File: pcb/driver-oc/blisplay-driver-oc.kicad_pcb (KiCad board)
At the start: 2 copper layers, 38 x 9 mm, 13 parts, among them J2 Flex, J3 Flex, J4 Flex, J5 Flex, U1 NCV7751

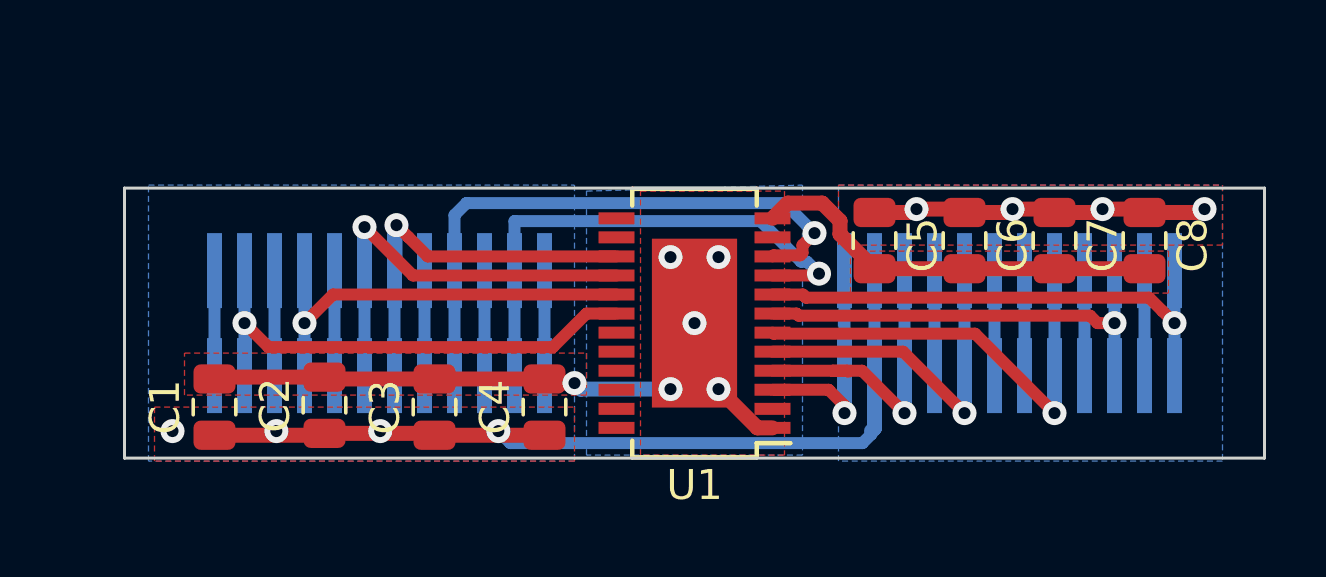
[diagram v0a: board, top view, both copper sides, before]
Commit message: Add simple connector to driver board.
This is not mirror symmetric which would be nicer for hassle-free
wiring. Maybe there should be two variants.
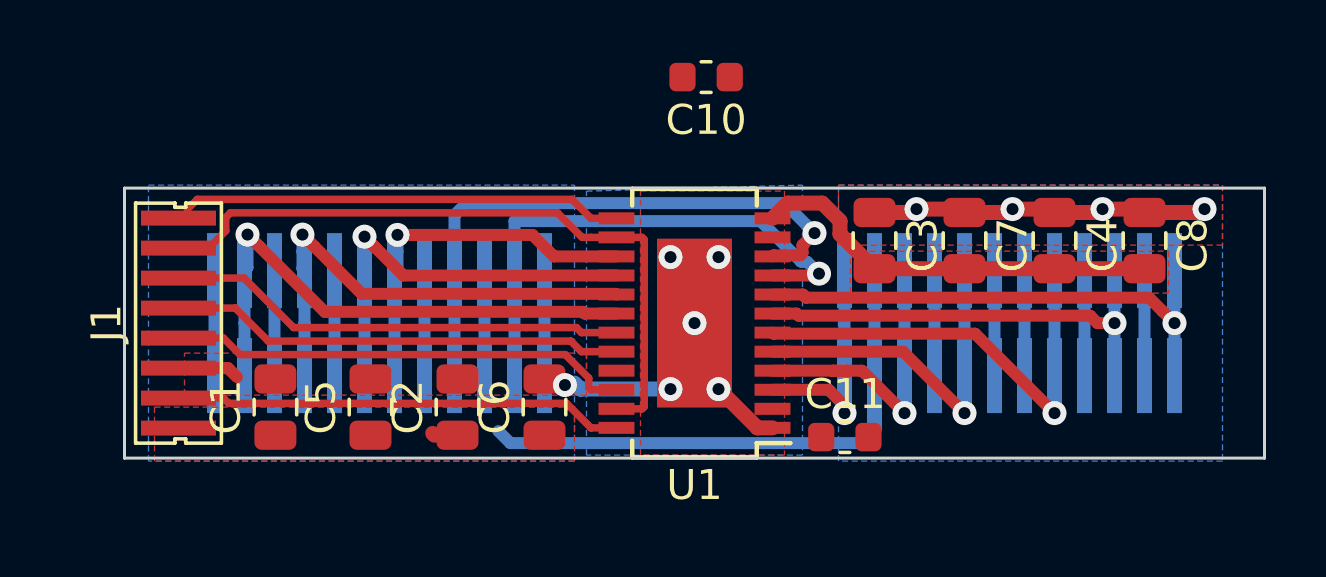
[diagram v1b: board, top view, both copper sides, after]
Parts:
- added C10: 100n, Capacitor_SMD:C_0603_1608Metric, F.Cu at (119.4, 46.3)
- added C11: 100n, Capacitor_SMD:C_0603_1608Metric, F.Cu at (124.0, 58.3)
- added J1: Conn_01x08, blisplay:driver-connect, F.Cu at (101.8, 54.5)
- moved C1 2.03 mm to (105.0, 57.3)
- moved C5 1.53 mm to (108.2, 57.3)
- moved C2 0.77 mm to (111.1, 57.3)
- renumbered C3 to C2, C5 to C3, C7 to C4, C2 to C5, C4 to C6, C6 to C7
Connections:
- U1 pad 14: Net-(U1-Pad14) -> /~CS
- U1 pad 19: Net-(U1-Pad19) -> /SO
- U1 pad 20: Net-(U1-Pad20) -> /SCK
- U1 pad 22: Net-(U1-Pad22) -> /SI
- U1 pad 23: Net-(U1-Pad23) -> /~CS
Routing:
- net /~CS: track 0.00 -> 23.2 mm
- net /SI: track 0.00 -> 15.5 mm
- net /SO: track 0.00 -> 15.4 mm
- net /SCK: track 0.00 -> 15.2 mm
- net VDDA: track 0.00 -> 15.0 mm
- net VDD: track 0.00 -> 14.7 mm
- net /VCOIL: track 79.1 -> 68.1 mm, vias 8 -> 4
- net GND: track 34.0 -> 24.2 mm
- net Net-(J3-Pad9): track 14.3 -> 16.0 mm
- net Net-(J3-Pad11): track 16.7 -> 18.1 mm

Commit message: Initial, fully routed version of open collector driver.
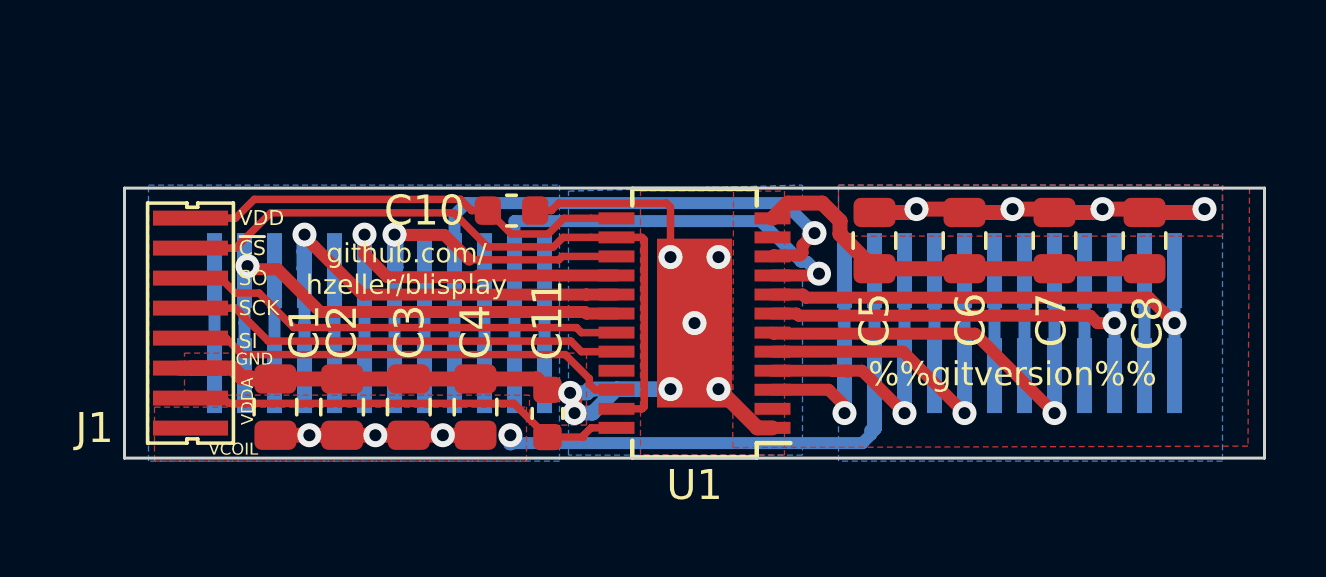
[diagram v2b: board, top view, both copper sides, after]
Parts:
- removed the C2 at (111.1, 57.3)
- added C3: 10μ, Capacitor_SMD:C_0805_2012Metric, F.Cu at (109.5, 57.3)
- moved C11 9.94 mm to (114.1, 57.5), turned to 90 degrees
- moved C10 7.87 mm to (112.9, 50.8), turned to 0 degrees
- moved C4 2.30 mm to (111.7, 57.3)
- moved C2 0.95 mm to (107.3, 57.3)
- moved J1 0.40 mm to (102.2, 54.5)
- renumbered C5 to C2, C6 to C4, C3 to C5, C7 to C6, C4 to C7
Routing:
- net GND: track 24.2 -> 46.9 mm, vias 6 -> 7
- net /VCOIL: track 68.1 -> 74.3 mm, vias 4 -> 8
- net Net-(J3-Pad11): track 18.1 -> 16.5 mm
- net Net-(J3-Pad6): track 12.3 -> 13.0 mm
- net /~CS: track 23.2 -> 23.8 mm
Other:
- net class Default: clearance 0.2 -> 0.18
- rule trace_clearance: 0.2 -> 0.18
- board text added: "%%gitversion%%"
- board text added: "GND"
- board text added: "SCK"
- board text added: "SI"
- board text added: "SO"
- board text added: "VCOIL"
- board text added: "VDD"
- board text added: "VDDA"
- board text added: "github.com/ hzeller/blisplay"
- board text added: "~CS"

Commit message: Label coil circuits. Pull EN to VDD.
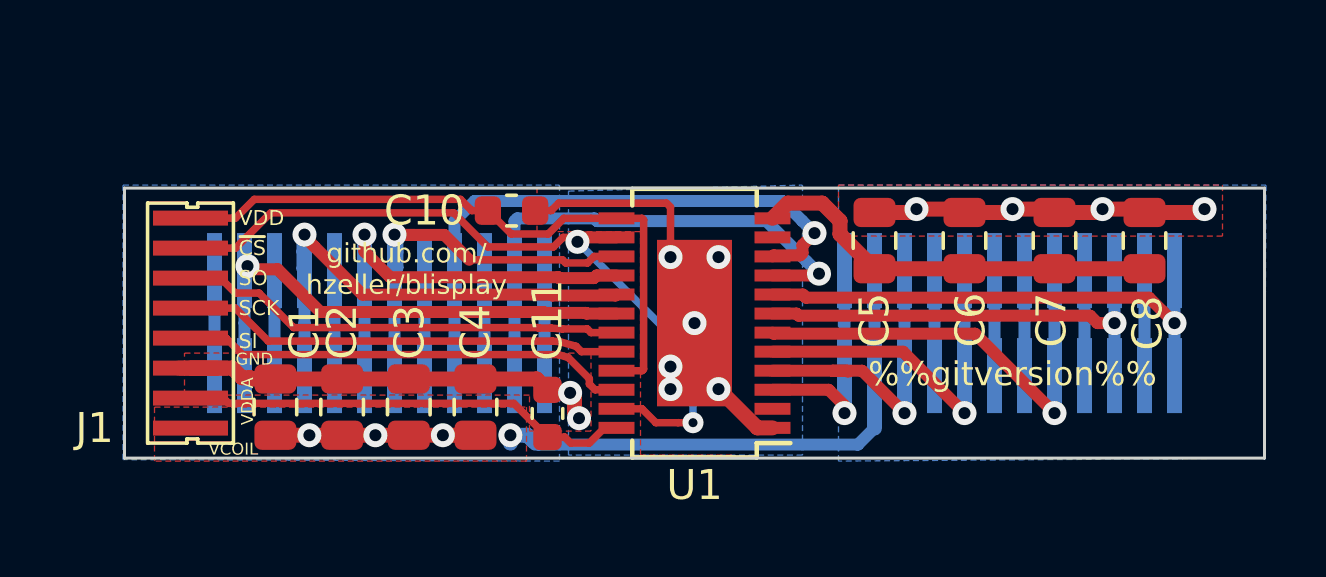
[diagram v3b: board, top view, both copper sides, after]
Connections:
- net Net-(J2-Pad1) renamed /Coil_1
- net Net-(J2-Pad10) renamed /Coil_5
- net Net-(J2-Pad12) renamed /Coil_6
- net Net-(J2-Pad3) renamed /Coil_2
- net Net-(J2-Pad5) renamed /Coil_3
- net Net-(J2-Pad8) renamed /Coil_4
- net Net-(J3-Pad11) renamed /Coil_12
- net Net-(J3-Pad2) renamed /Coil_7
- net Net-(J3-Pad4) renamed /Coil_8
- net Net-(J3-Pad6) renamed /Coil_9
- net Net-(J3-Pad7) renamed /Coil_10
- net Net-(J3-Pad9) renamed /Coil_11
- U1 pad 21: Net-(U1-Pad21) -> VDD
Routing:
- net GND: track 46.9 -> 40.0 mm, vias 7 -> 8
- net VDD: track 15.2 -> 22.0 mm
- net /~CS: track 23.8 -> 28.0 mm, vias 0 -> 2
